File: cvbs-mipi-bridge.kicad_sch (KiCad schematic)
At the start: 107 parts, among them IC1 ADV7282-M, IC2 TLV70018, IC4 SN74AUP1G17DCKR, IC5 SN74AUP1G17DCKR, J1 WE_68715014522, J2 1053131102, J3 KLPX-0848A-2-Y, J4 KLPX-0848A-2-Y, J5 KLPX-0848A-2-Y, J6 KLPX-0848A-2-Y, J7 61300211121, Q1 BSS138APW, Q2 BSS138APW, Q3 BSS138APW, Q4 BSS138APW, Y1 ABM8G-28.63636MHZ-18-D2Y-T

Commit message: Update naming convention, assign revision 1.0.0, update signage on PCB
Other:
- company: Antmicro Ltd. -> (none)
- title: ModADV7282-M -> CVBS-MIPI Bridge
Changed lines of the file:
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@@
   (paper "A3")
   (title_block
-    (title "ModADV7282-M")
-    (rev "1.2.0")
-    (company "Antmicro Ltd.")
+    (title "CVBS-MIPI Bridge")
+    (date "2022-09-29")
+    (rev "1.0.0")
+    (comment 1 "www.antmicro.com")
+    (comment 2 "Antmicro Ltd.")
   )
   (junction (at 69.088 115.57) (diameter 0) (color 0 0 0 0)

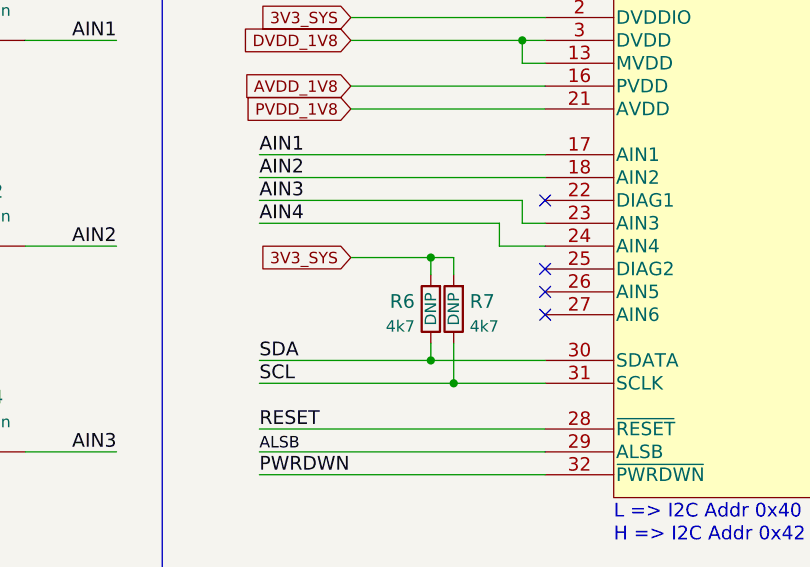
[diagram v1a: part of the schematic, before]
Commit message: Testpoints added
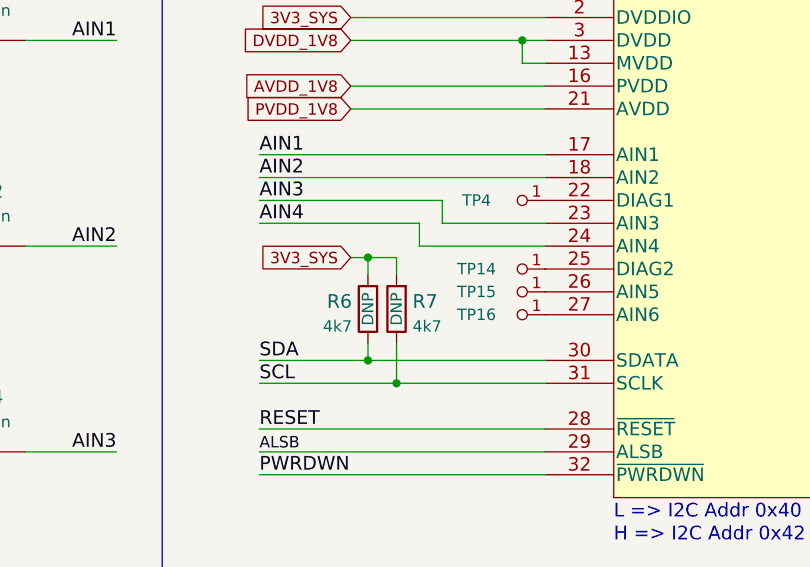
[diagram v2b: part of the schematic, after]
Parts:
- added TP14, TP15, TP16, TP4: TP, cvbs-mipi-bridge-footprints:TP-R-1.5, symbol cvbs-mipi-bridge:TP
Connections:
- net at IC1.22 (DIAG1): now also TP4.1
- net at IC1.25 (DIAG2): now also TP14.1
- net at IC1.26 (AIN5): now also TP15.1
- net at IC1.27 (AIN6): now also TP16.1
- no-connect marks 39 -> 35
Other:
- moved on the sheet: R6, R7

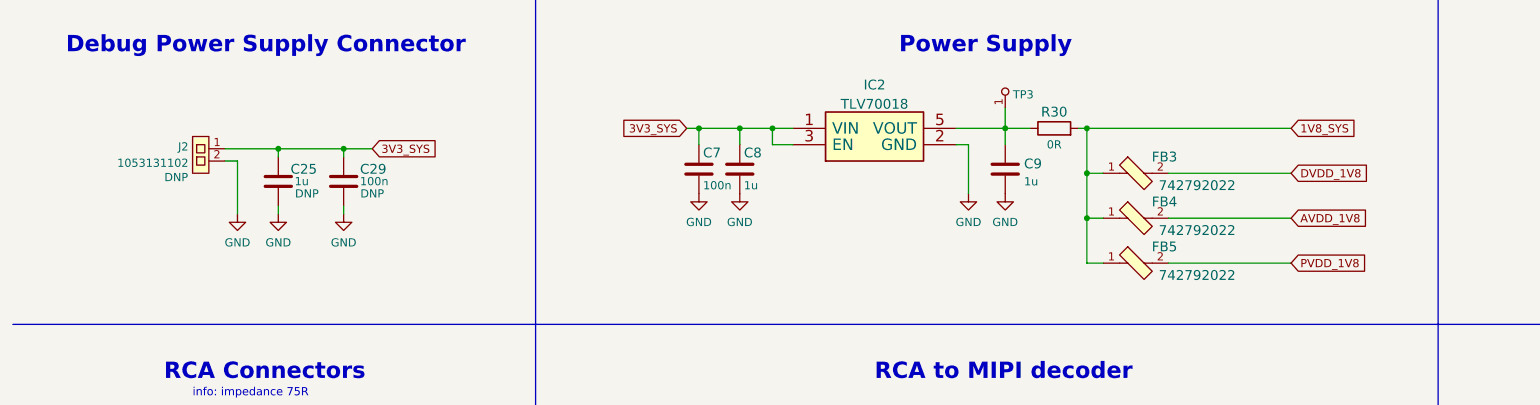
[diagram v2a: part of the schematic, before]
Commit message: Add coupling capacitors
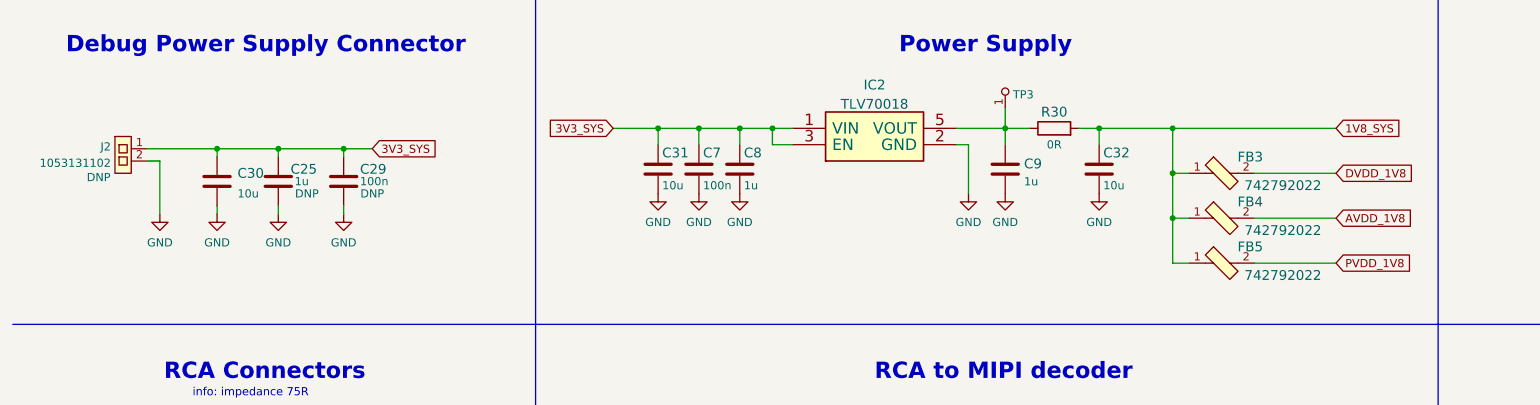
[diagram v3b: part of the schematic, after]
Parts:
- added C30, C31, C32: C_10u_0603, cvbs-mipi-bridge-footprints:0603-cap, symbol cvbs-mipi-bridge:C_10u_0603
- IC1: footprint antmicro-footprints:LFCSP-32-1EP-5x5mm -> cvbs-mipi-bridge-footprints:LFCSP-32-1EP-5x5mm; symbol antmicroDataAcquisitionAnalogtoDigitalConvertersADC:ADV7282-M -> cvbs-mipi-bridge:ADV7282-M
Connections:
- net 1V8_SYS: now also C32.1
- net 3V3_SYS: now also C30.1, C31.1
- net GND: now also C30.2, C31.2, C32.2
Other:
- moved on the sheet: FB3, FB4, FB5, J2

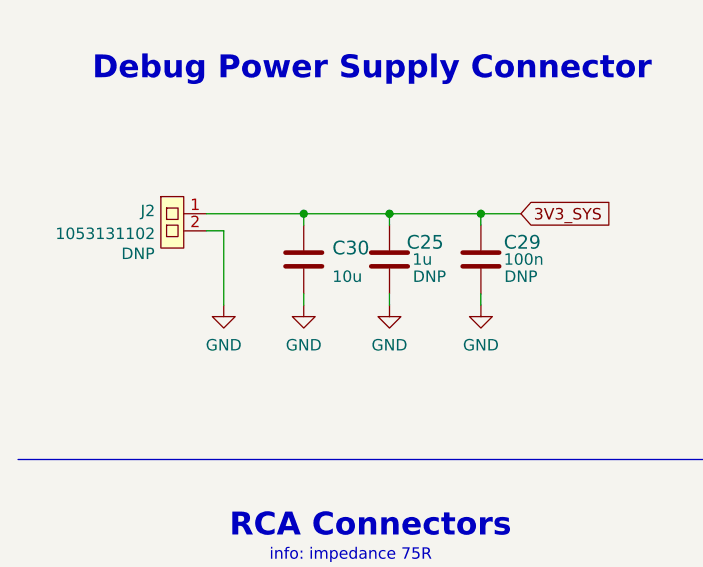
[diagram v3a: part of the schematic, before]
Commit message: Mark C30 as DNP, improve it's clarity on schematic
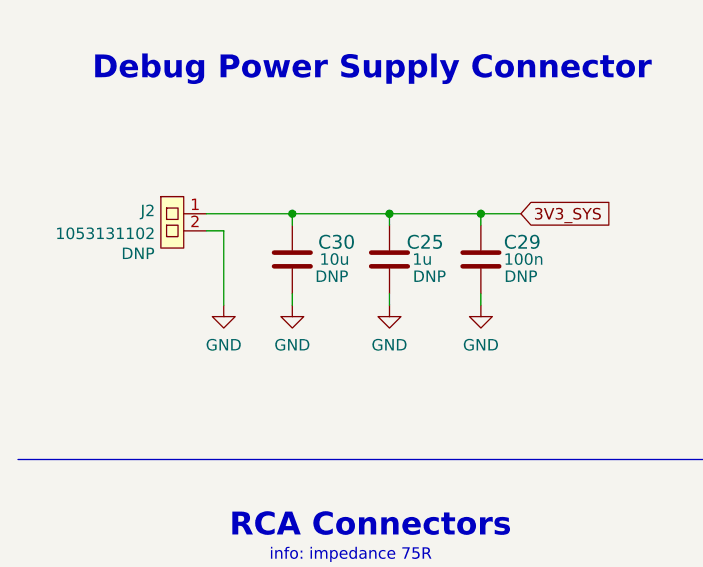
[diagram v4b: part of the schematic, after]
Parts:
- C30: DNP (none) -> DNP
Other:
- moved on the sheet: C30
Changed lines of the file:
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@@
   (junction (at 125.73 36.83) (diameter 0) (color 0 0 0 0)
   )
+  (junction (at 43.18 40.005) (diameter 0) (color 0 0 0 0)
+  )
   (junction (at 117.475 262.255) (diameter 0) (color 0 0 0 0)
   )
   (junction (at 116.84 116.84) (diameter 0) (color 0 0 0 0)
   )
-  (junction (at 44.45 40.005) (diameter 0) (color 0 0 0 0)
-  )
   (junction (at 156.21 249.555) (diameter 0) (color 0 0 0 0)
   )
@@
     (stroke (width 0) (type default) (color 0 0 0 0))
   )
-  (wire (pts (xy 33.655 40.005) (xy 44.45 40.005))
-    (stroke (width 0) (type default) (color 0 0 0 0))
-  )
   (wire (pts (xy 277.495 213.36) (xy 277.495 210.82))
     (stroke (width 0) (type default) (color 0 0 0 0))
@@
     (stroke (width 0) (type default) (color 0 0 0 0))
   )
-  (wire (pts (xy 44.45 40.005) (xy 44.45 41.275))
+  (wire (pts (xy 43.18 40.005) (xy 43.18 41.275))
     (stroke (width 0) (type default) (color 0 0 0 0))
   )
@@
     (stroke (width 0) (type default) (color 0 0 0 0))
   )
-  (wire (pts (xy 44.45 48.895) (xy 44.45 50.165))
+  (wire (pts (xy 43.18 48.895) (xy 43.18 50.165))
     (stroke (width 0) (type default) (color 0 0 0 0))
   )
@@
     (stroke (width 0) (type default) (color 0 0 0 0))
   )
-  (wire (pts (xy 44.45 40.005) (xy 53.975 40.005))
+  (wire (pts (xy 43.18 40.005) (xy 53.975 40.005))
     (stroke (width 0) (type default) (color 0 0 0 0))
   )
@@
     (stroke (width 0) (type default) (color 0 0 0 0))
   )
+  (wire (pts (xy 33.655 40.005) (xy 43.18 40.005))
+    (stroke (width 0) (type default) (color 0 0 0 0))
+  )
   (image (at 73.18 272.78) (scale 0.15)
     (data
@@
     (pin "K")
   )
-  (symbol (lib_id "cvbs-mipi-bridge:GND") (at 44.45 50.165 0) (mirror y) (unit 1)
+  (symbol (lib_id "cvbs-mipi-bridge:GND") (at 43.18 50.165 0) (mirror y) (unit 1)
     (in_bom yes) (on_board yes) (fields_autoplaced)
-    (property "Reference" "#PWR08" (id 0) (at 44.45 56.515 0)
+    (property "Reference" "#PWR08" (id 0) (at 43.18 56.515 0)
       (effects (font (size 1.27 1.27)) hide)
     )
-    (property "Value" "GND" (id 1) (at 44.45 54.6084 0))
-    (property "Footprint" "" (id 2) (at 44.45 50.165 0)
+    (property "Value" "GND" (id 1) (at 43.18 54.6084 0))
+    (property "Footprint" "" (id 2) (at 43.18 50.165 0)
       (effects (font (size 1.27 1.27)) hide)
     )
-    (property "Datasheet" "" (id 3) (at 44.45 50.165 0)
+    (property "Datasheet" "" (id 3) (at 43.18 50.165 0)
       (effects (font (size 1.27 1.27)) hide)
     )
@@
     (pin "2")
   )
-  (symbol (lib_id "cvbs-mipi-bridge:C_10u_0603") (at 44.45 45.085 0) (unit 1)
-    (in_bom yes) (on_board yes) (fields_autoplaced)
-    (property "Reference" "C30" (id 0) (at 47.625 43.815 0)
-      (effects (font (size 1.524 1.524)) (justify left))
+  (symbol (lib_id "cvbs-mipi-bridge:C_10u_0603") (at 43.18 45.085 0) (unit 1)
+    (in_bom yes) (on_board yes)
+    (property "Reference" "C30" (id 0) (at 50.165 43.18 0)
+      (effects (font (size 1.524 1.524)) (justify right))
     )
-    (property "Value" "C_10u_0603" (id 1) (at 44.45 48.895 0)
+    (property "Value" "C_10u_0603" (id 1) (at 43.18 48.895 0)
       (effects (font (size 1.524 1.524)) hide)
     )
-    (property "Footprint" "cvbs-mipi-bridge-footprints:0603-cap" (id 2) (at 49.53 40.005 0)
+    (property "Footprint" "cvbs-mipi-bridge-footprints:0603-cap" (id 2) (at 48.26 40.005 0)
       (effects (font (size 1.524 1.524)) (justify left) hide)
     )
-    (property "Datasheet" "" (id 3) (at 44.45 45.085 0)
+    (property "Datasheet" "" (id 3) (at 43.18 45.085 0)
       (effects (font (size 1.27 1.27)) hide)
     )
-    (property "Manufacturer" "Murata" (id 4) (at 49.53 34.925 0)
+    (property "Manufacturer" "Murata" (id 4) (at 48.26 34.925 0)
       (effects (font (size 1.524 1.524)) (justify left) hide)
     )
-    (property "MPN" "GRM188R61A106KE69D" (id 5) (at 49.53 37.465 0)
+    (property "MPN" "GRM188R61A106KE69D" (id 5) (at 48.26 37.465 0)
       (effects (font (size 1.524 1.524)) (justify left) hide)
     )
-    (property "Val" "10u" (id 6) (at 47.625 46.9899 0)
+    (property "Val" "10u" (id 6) (at 49.53 45.085 0)
+      (effects (font (size 1.27 1.27)) (justify right))
+    )
+    (property "DNP" "DNP" (id 7) (at 45.72 46.99 0)
       (effects (font (size 1.27 1.27)) (justify left))
     )

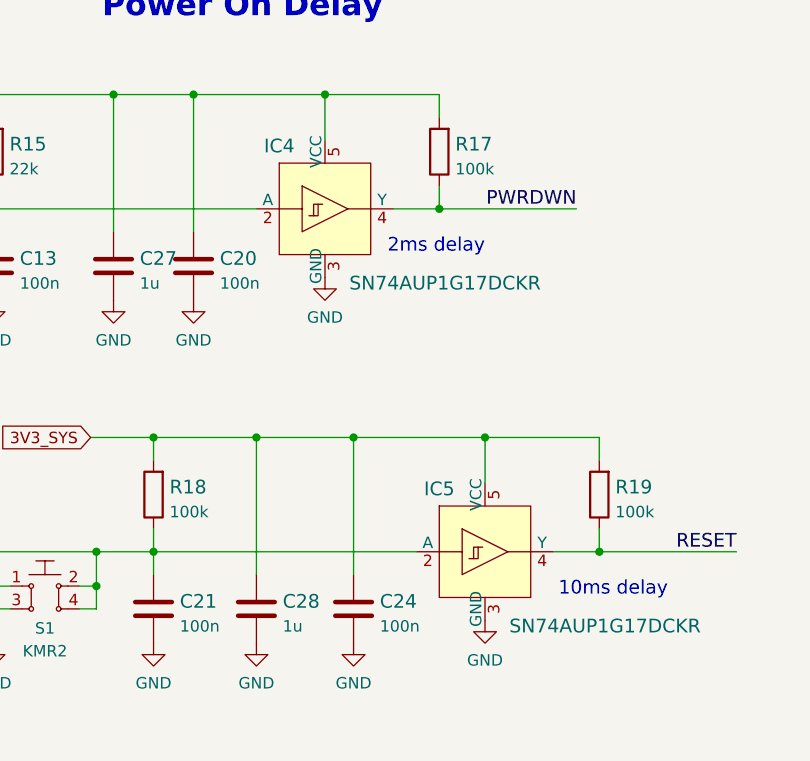
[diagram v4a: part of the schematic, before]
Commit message: Update SN74AUP1G17DCKR symbol on SCH from local library
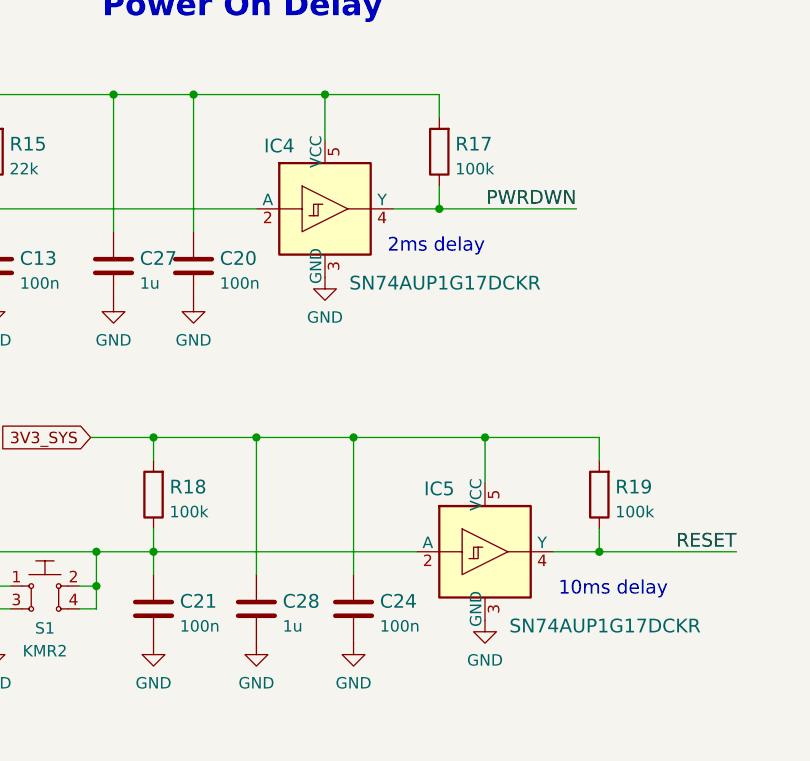
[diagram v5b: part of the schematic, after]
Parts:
- IC4, IC5: footprint cvbs-mipi-bridge-footprints:SOT-753 -> antmicro-footprints:SC-70-5
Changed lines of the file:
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@@
     (pin "2")
   )
-  (symbol (lib_id "cvbs-mipi-bridge:SN74AUP1G17DCKR") (at 193.04 262.255 0) (unit 1)
+  (symbol (lib_name "SN74AUP1G17DCKR_1") (lib_id "cvbs-mipi-bridge:SN74AUP1G17DCKR") (at 193.04 262.255 0) (unit 1)
     (in_bom yes) (on_board yes)
     (property "Reference" "IC5" (id 0) (at 187.96 255.27 0)
@@
       (effects (font (size 1.524 1.524)))
     )
-    (property "Footprint" "cvbs-mipi-bridge-footprints:SOT-753" (id 2) (at 198.12 257.175 0)
+    (property "Footprint" "antmicro-footprints:SC-70-5" (id 2) (at 198.12 257.175 0)
       (effects (font (size 1.524 1.524)) (justify left) hide)
     )
-    (property "Datasheet" "http://www.ti.com/general/docs/suppproductinfo.tsp?distId=10&gotoUrl=http%3A%2F%2Fwww.ti.com%2Flit%2Fgpn%2Fsn74lvc1g07" (id 3) (at 198.12 254.635 0)
+    (property "Datasheet" "https://www.ti.com/lit/ds/symlink/sn74aup1g17.pdf" (id 3) (at 198.12 254.635 0)
       (effects (font (size 1.524 1.524)) (justify left) hide)
     )
@@
       (effects (font (size 1.524 1.524)))
     )
-    (property "Footprint" "cvbs-mipi-bridge-footprints:SOT-753" (id 2) (at 180.34 219.075 0)
+    (property "Footprint" "antmicro-footprints:SC-70-5" (id 2) (at 180.34 219.075 0)
       (effects (font (size 1.524 1.524)) (justify left) hide)
     )
-    (property "Datasheet" "http://www.ti.com/general/docs/suppproductinfo.tsp?distId=10&gotoUrl=http%3A%2F%2Fwww.ti.com%2Flit%2Fgpn%2Fsn74lvc1g07" (id 3) (at 180.34 216.535 0)
+    (property "Datasheet" "https://www.ti.com/lit/ds/symlink/sn74aup1g17.pdf" (id 3) (at 180.34 216.535 0)
       (effects (font (size 1.524 1.524)) (justify left) hide)
     )
@@
     )
     (path "/e9bc5ab4-176e-40e0-b923-d99288556834"
-      (reference "IC4") (unit 1) (value "SN74AUP1G17DCKR") (footprint "cvbs-mipi-bridge-footprints:SOT-753")
+      (reference "IC4") (unit 1) (value "SN74AUP1G17DCKR") (footprint "antmicro-footprints:SC-70-5")
     )
     (path "/28694f0f-765a-4a51-9c52-76a4485352d8"
-      (reference "IC5") (unit 1) (value "SN74AUP1G17DCKR") (footprint "cvbs-mipi-bridge-footprints:SOT-753")
+      (reference "IC5") (unit 1) (value "SN74AUP1G17DCKR") (footprint "antmicro-footprints:SC-70-5")
     )
     (path "/cccea5dc-95b3-4bdd-bdf0-97c0ee0354cd"
